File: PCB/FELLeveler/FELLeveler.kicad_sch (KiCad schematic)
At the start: 15 parts, among them J1 PRG0, J2 PRG1, T1 VCC IN, U1 ESP32-WROOM-32

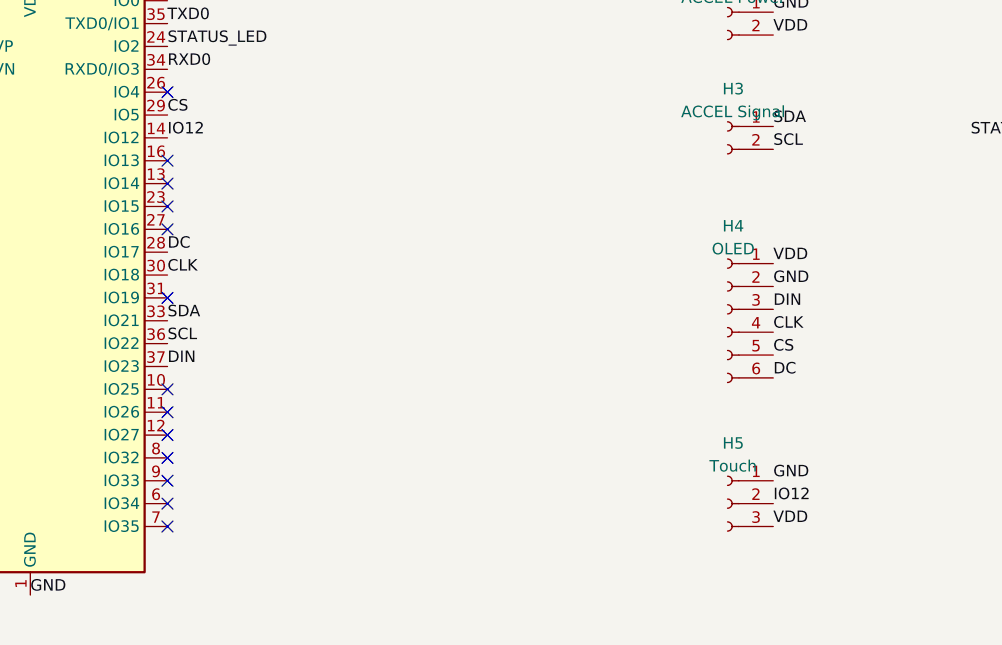
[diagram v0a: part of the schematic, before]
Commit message: Added Boot pin, tweaked PCB
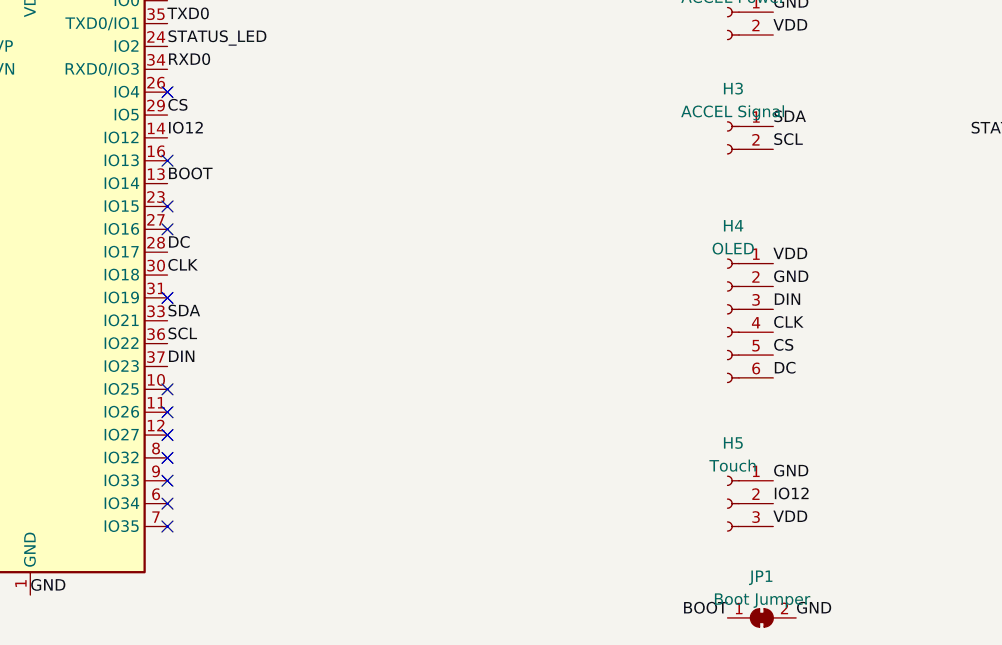
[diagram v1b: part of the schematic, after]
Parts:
- added JP1: Boot Jumper, Jumper:SolderJumper-2_P1.3mm_Bridged_Pad1.0x1.5mm, symbol Jumper:SolderJumper_2_Bridged
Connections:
- net GND: now also JP1.2 (B)
- net BOOT: now reaches U1.13 (IO14)
- net BOOT: now also JP1.1 (A)
- no-connect marks 22 -> 21
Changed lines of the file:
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@@
   (no_connect (at 66.04 111.76))
   (no_connect (at 66.04 121.92))
-  (no_connect (at 66.04 99.06))
   (no_connect (at 66.04 137.16))
   (no_connect (at 35.56 111.76))
@@
     (effects (font (size 1.27 1.27)) (justify left bottom))
   )
+  (label "BOOT" (at 66.04 99.06 0)
+    (effects (font (size 1.27 1.27)) (justify left bottom))
+  )
   (label "SCL" (at 66.04 116.84 0)
     (effects (font (size 1.27 1.27)) (justify left bottom))
@@
   (label "STATUS_LED" (at 66.04 83.82 0)
     (effects (font (size 1.27 1.27)) (justify left bottom))
+  )
+  (label "BOOT" (at 128.27 147.32 180)
+    (effects (font (size 1.27 1.27)) (justify right bottom))
   )
   (label "GND" (at 167.64 43.18 0)
@@
   (label "EN" (at 35.56 78.74 180)
     (effects (font (size 1.27 1.27)) (justify right bottom))
+  )
+  (label "GND" (at 135.89 147.32 0)
+    (effects (font (size 1.27 1.27)) (justify left bottom))
   )
   (symbol (lib_id "RF_Module:ESP32-WROOM-32") (at 50.8 109.22 0) (unit 1)
@@
     (pin "3")
   )
+  (symbol (lib_id "Jumper:SolderJumper_2_Bridged") (at 132.08 147.32 0) (unit 1)
+    (in_bom yes) (on_board yes) (fields_autoplaced)
+    (property "Reference" "JP1" (id 0) (at 132.08 142.7312 0))
+    (property "Value" "Boot Jumper" (id 1) (at 132.08 145.2681 0))
+    (property "Footprint" "Jumper:SolderJumper-2_P1.3mm_Bridged_Pad1.0x1.5mm" (id 2) (at 132.08 147.32 0)
+      (effects (font (size 1.27 1.27)) hide)
+    )
+    (property "Datasheet" "~" (id 3) (at 132.08 147.32 0)
+      (effects (font (size 1.27 1.27)) hide)
+    )
+    (pin "1")
+    (pin "2")
+  )
   (sheet_instances
     (path "/" (page "1"))
@@
       (reference "J2") (unit 1) (value "PRG1") (footprint "Connector_PinHeader_2.54mm:PinHeader_1x03_P2.54mm_Vertical")
     )
+    (path "/ed76cb21-0b5e-4ca2-8075-7e28e38e7199"
+      (reference "JP1") (unit 1) (value "Boot Jumper") (footprint "Jumper:SolderJumper-2_P1.3mm_Bridged_Pad1.0x1.5mm")
+    )
     (path "/00000000-0000-0000-0000-0000617682ca"

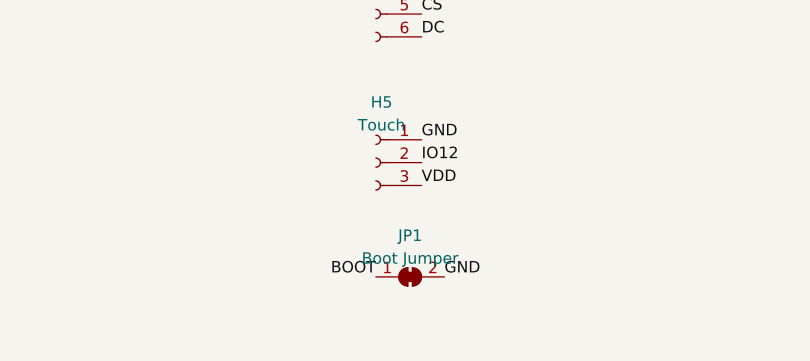
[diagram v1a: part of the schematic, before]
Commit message: Tweaked PCB, submitted v1.0 to fab.
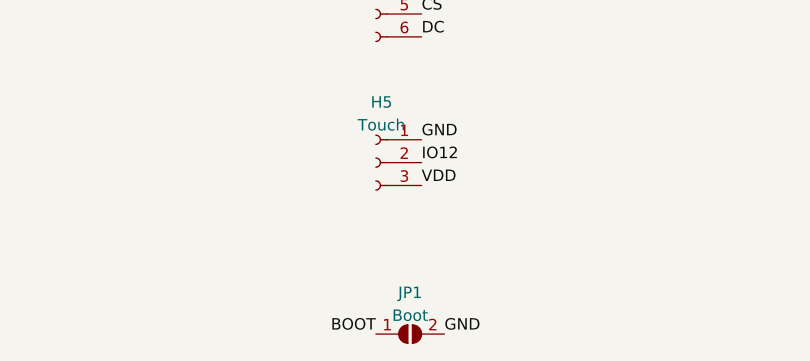
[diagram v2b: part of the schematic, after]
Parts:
- removed JP1: Boot Jumper, Jumper:SolderJumper-2_P1.3mm_Bridged_Pad1.0x1.5mm, symbol Jumper:SolderJumper_2_Bridged
- added JP1: Boot, Jumper:SolderJumper-2_P1.3mm_Open_Pad1.0x1.5mm, symbol Jumper:SolderJumper_2_Open
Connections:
- net BOOT: now also JP1.1 (A)
- net GND: now also JP1.2 (B)
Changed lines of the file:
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@@
     (effects (font (size 1.27 1.27)) (justify left bottom))
   )
-  (label "BOOT" (at 128.27 147.32 180)
+  (label "BOOT" (at 128.27 153.67 180)
     (effects (font (size 1.27 1.27)) (justify right bottom))
   )
@@
     (effects (font (size 1.27 1.27)) (justify right bottom))
   )
-  (label "GND" (at 135.89 147.32 0)
+  (label "GND" (at 135.89 153.67 0)
     (effects (font (size 1.27 1.27)) (justify left bottom))
   )
@@
     (pin "3")
   )
-  (symbol (lib_id "Jumper:SolderJumper_2_Bridged") (at 132.08 147.32 0) (unit 1)
+  (symbol (lib_id "Jumper:SolderJumper_2_Open") (at 132.08 153.67 0) (unit 1)
     (in_bom yes) (on_board yes) (fields_autoplaced)
-    (property "Reference" "JP1" (id 0) (at 132.08 142.7312 0))
-    (property "Value" "Boot Jumper" (id 1) (at 132.08 145.2681 0))
-    (property "Footprint" "Jumper:SolderJumper-2_P1.3mm_Bridged_Pad1.0x1.5mm" (id 2) (at 132.08 147.32 0)
-      (effects (font (size 1.27 1.27)) hide)
-    )
-    (property "Datasheet" "~" (id 3) (at 132.08 147.32 0)
+    (property "Reference" "JP1" (id 0) (at 132.08 149.0812 0))
+    (property "Value" "Boot" (id 1) (at 132.08 151.6181 0))
+    (property "Footprint" "Jumper:SolderJumper-2_P1.3mm_Open_Pad1.0x1.5mm" (id 2) (at 132.08 153.67 0)
+      (effects (font (size 1.27 1.27)) hide)
+    )
+    (property "Datasheet" "~" (id 3) (at 132.08 153.67 0)
       (effects (font (size 1.27 1.27)) hide)
     )
@@
       (reference "J2") (unit 1) (value "PRG1") (footprint "Connector_PinHeader_2.54mm:PinHeader_1x03_P2.54mm_Vertical")
     )
-    (path "/ed76cb21-0b5e-4ca2-8075-7e28e38e7199"
-      (reference "JP1") (unit 1) (value "Boot Jumper") (footprint "Jumper:SolderJumper-2_P1.3mm_Bridged_Pad1.0x1.5mm")
+    (path "/f58742f8-e57e-4646-a6f5-0463e0eceeb8"
+      (reference "JP1") (unit 1) (value "Boot") (footprint "Jumper:SolderJumper-2_P1.3mm_Open_Pad1.0x1.5mm")
     )
     (path "/00000000-0000-0000-0000-0000617682ca"
